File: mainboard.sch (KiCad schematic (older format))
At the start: 42 parts

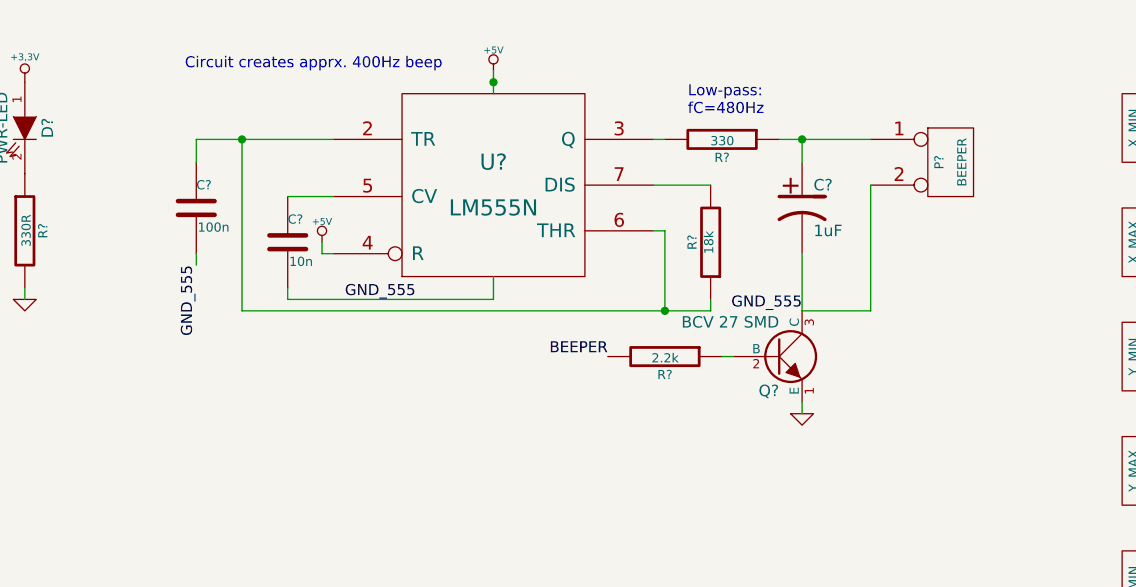
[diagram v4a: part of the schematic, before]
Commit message: Removed 555-Timer-Circuit. Added Opamp to drive beeper.
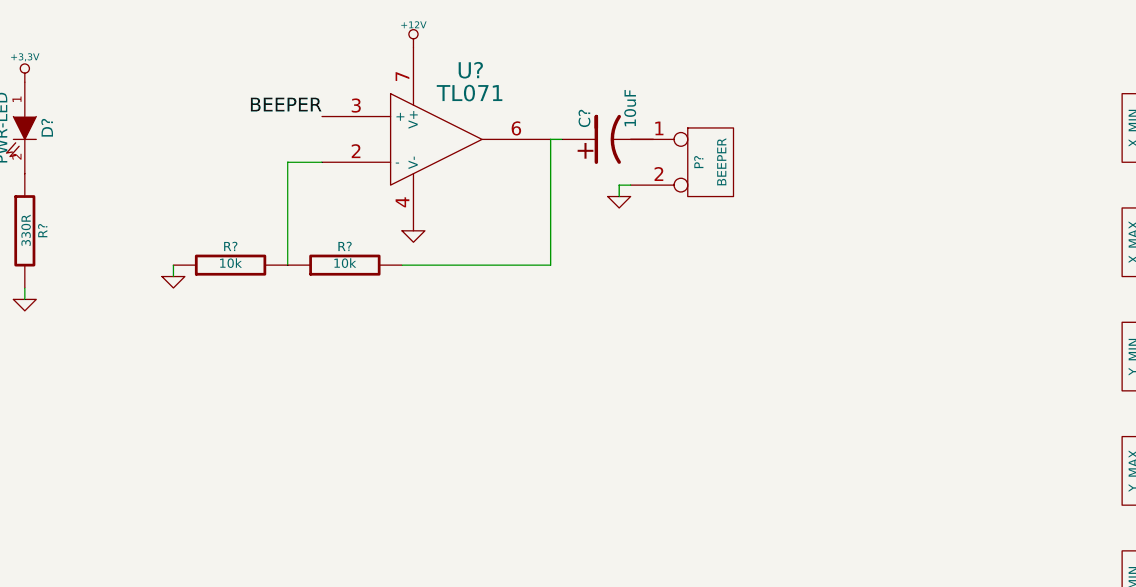
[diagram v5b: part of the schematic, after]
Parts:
- removed C?: 1uF, ~, symbol CP1
- removed C?: 100n, ~, symbol C
- removed C?: 10n, ~, symbol C
- removed P?: BEEPER, symbol CONN_2
- removed Q?: BCV 27 SMD, symbol NPN
- removed R?: 330, symbol R
- removed R?: 18k, symbol R
- removed R?: 2.2k, symbol R
- removed U?: LM555N, symbol LM555N
- added C?: 10uF, ~, symbol CP1
- added P?: BEEPER, symbol CONN_2
- added R? (x2): 10k, symbol R
- added U?: TL071, symbol TL071
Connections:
- net labels removed: GND_555
- wire segments 170 -> 154
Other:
- note removed: "Circuit creates apprx. 400Hz beep"
- note removed: "Low-pass:\nfC=480Hz"
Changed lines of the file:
@@
 Connection ~ 9800 5550
 $Comp
-L LM555N U?
-U 1 1 53348D69
-P 5150 1350
-F 0 "U?" H 5150 1450 70  0000 C CNN
-F 1 "LM555N" H 5150 1250 70  0000 C CNN
-F 2 "" H 5150 1350 60  0000 C CNN
-F 3 "" H 5150 1350 60  0000 C CNN
-	1    5150 1350
+L TL071 U?
+U 1 1 5335F113
+P 4900 1150
+F 0 "U?" H 5050 1450 70  0000 C CNN
+F 1 "TL071" H 5050 1350 70  0000 C CNN
+F 2 "" H 4900 1150 60  0000 C CNN
+F 3 "" H 4900 1150 60  0000 C CNN
+	1    4900 1150
+	1    0    0    -1
+$EndComp
+$Comp
+L R R?
+U 1 1 5335F295
+P 4000 1700
+F 0 "R?" V 4080 1700 40  0000 C CNN
+F 1 "10k" V 4007 1701 40  0000 C CNN
+F 2 "" V 3930 1700 30  0000 C CNN
+F 3 "" H 4000 1700 30  0000 C CNN
+	1    4000 1700
+	0    -1   -1   0
+$EndComp
+Wire Wire Line
+	4250 1250 4400 1250
+$Comp
+L GND #PWR?
+U 1 1 5335F4AF
+P 3750 1750
+F 0 "#PWR?" H 3750 1750 30  0001 C CNN
+F 1 "GND" H 3750 1680 30  0001 C CNN
+F 2 "" H 3750 1750 60  0000 C CNN
+F 3 "" H 3750 1750 60  0000 C CNN
+	1    3750 1750
 	1    0    0    -1
 $EndComp
 Wire Wire Line
-	5150 1850 5150 1750
+	3750 1750 3750 1700
 $Comp
-L +5V #PWR?
-U 1 1 533493FF
-P 5150 850
-F 0 "#PWR?" H 5150 940 20  0001 C CNN
-F 1 "+5V" H 5150 940 30  0000 C CNN
-F 2 "" H 5150 850 60  0000 C CNN
-F 3 "" H 5150 850 60  0000 C CNN
-	1    5150 850
+L R R?
+U 1 1 5335F56E
+P 4500 1700
+F 0 "R?" V 4580 1700 40  0000 C CNN
+F 1 "10k" V 4507 1701 40  0000 C CNN
+F 2 "" V 4430 1700 30  0000 C CNN
+F 3 "" H 4500 1700 30  0000 C CNN
+	1    4500 1700
+	0    -1   -1   0
+$EndComp
+Wire Wire Line
+	4750 1700 5400 1700
+Text Label 4400 1050 2    60   ~ 0
+BEEPER
+$Comp
+L GND #PWR?
+U 1 1 5335F918
+P 4800 1550
+F 0 "#PWR?" H 4800 1550 30  0001 C CNN
+F 1 "GND" H 4800 1480 30  0001 C CNN
+F 2 "" H 4800 1550 60  0000 C CNN
+F 3 "" H 4800 1550 60  0000 C CNN
+	1    4800 1550
+	1    0    0    -1
+$EndComp
+$Comp
+L +12V #PWR?
+U 1 1 5335F923
+P 4800 750
+F 0 "#PWR?" H 4800 700 20  0001 C CNN
+F 1 "+12V" H 4800 850 30  0000 C CNN
+F 2 "" H 4800 750 60  0000 C CNN
+F 3 "" H 4800 750 60  0000 C CNN
+	1    4800 750
+	1    0    0    -1
+$EndComp
+$Comp
+L CONN_2 P?
+U 1 1 5335FA9A
+P 6100 1250
+F 0 "P?" V 6050 1250 40  0000 C CNN
+F 1 "BEEPER" V 6150 1250 40  0000 C CNN
+F 2 "" H 6100 1250 60  0000 C CNN
+F 3 "" H 6100 1250 60  0000 C CNN
+	1    6100 1250
+	1    0    0    -1
+$EndComp
+$Comp
+L CP1 C?
+U 1 1 5335FAAC
+P 5650 1150
+F 0 "C?" H 5700 1250 50  0000 L CNN
+F 1 "10uF" H 5700 1050 50  0000 L CNN
+F 2 "~" H 5650 1150 60  0000 C CNN
+F 3 "~" H 5650 1150 60  0000 C CNN
+	1    5650 1150
+	0    -1   -1   0
+$EndComp
+Wire Wire Line
+	5400 1150 5450 1150
+$Comp
+L GND #PWR?
+U 1 1 5335FB6A
+P 5700 1400
+F 0 "#PWR?" H 5700 1400 30  0001 C CNN
+F 1 "GND" H 5700 1330 30  0001 C CNN
+F 2 "" H 5700 1400 60  0000 C CNN
+F 3 "" H 5700 1400 60  0000 C CNN
+	1    5700 1400
 	1    0    0    -1
 $EndComp
 Wire Wire Line
-	5150 850  5150 950
-Connection ~ 5150 900
-$Comp
-L R R?
-U 1 1 53349632
-P 6150 1150
-F 0 "R?" V 6230 1150 40  0000 C CNN
-F 1 "330" V 6157 1151 40  0000 C CNN
-F 2 "" V 6080 1150 30  0000 C CNN
-F 3 "" H 6150 1150 30  0000 C CNN
-	1    6150 1150
-	0    1    1    0
-$EndComp
+	5700 1400 5700 1350
 Wire Wire Line
-	5900 1150 5850 1150
-$Comp
-L CP1 C?
-U 1 1 533496FD
-P 6500 1450
-F 0 "C?" H 6550 1550 50  0000 L CNN
-F 1 "1uF" H 6550 1350 50  0000 L CNN
-F 2 "~" H 6500 1450 60  0000 C CNN
-F 3 "~" H 6500 1450 60  0000 C CNN
-	1    6500 1450
-	1    0    0    -1
-$EndComp
+	5700 1350 5750 1350
 Wire Wire Line
-	6500 1250 6500 1150
+	5400 1700 5400 1150
 Wire Wire Line
-	6400 1150 6800 1150
-$Comp
-L GND #PWR?
-U 1 1 53349958
-P 6500 2350
-F 0 "#PWR?" H 6500 2350 30  0001 C CNN
-F 1 "GND" H 6500 2280 30  0001 C CNN
-F 2 "" H 6500 2350 60  0000 C CNN
-F 3 "" H 6500 2350 60  0000 C CNN
-	1    6500 2350
-	1    0    0    -1
-$EndComp
-Wire Wire Line
-	6500 1650 6500 1900
-Text Notes 6000 1050 0    48   ~ 0
-Low-pass:\nfC=480Hz
-$Comp
-L CONN_2 P?
-U 1 1 53349A50
-P 7150 1250
-F 0 "P?" V 7100 1250 40  0000 C CNN
-F 1 "BEEPER" V 7200 1250 40  0000 C CNN
-F 2 "" H 7150 1250 60  0000 C CNN
-F 3 "" H 7150 1250 60  0000 C CNN
-	1    7150 1250
-	1    0    0    -1
-$EndComp
-Connection ~ 6500 1150
-Wire Wire Line
-	6800 1350 6800 1900
-$Comp
-L +5V #PWR?
-U 1 1 53349CB7
-P 4400 1600
-F 0 "#PWR?" H 4400 1690 20  0001 C CNN
-F 1 "+5V" H 4400 1690 30  0000 C CNN
-F 2 "" H 4400 1600 60  0000 C CNN
-F 3 "" H 4400 1600 60  0000 C CNN
-	1    4400 1600
-	1    0    0    -1
-$EndComp
-Wire Wire Line
-	4450 1650 4400 1650
-Wire Wire Line
-	4400 1650 4400 1600
-Wire Wire Line
-	5850 1550 5900 1550
-Wire Wire Line
-	5900 1550 5900 1900
-Wire Wire Line
-	4050 1900 6100 1900
-Wire Wire Line
-	4050 1900 4050 1150
-Wire Wire Line
-	3850 1150 4450 1150
-$Comp
-L R R?
-U 1 1 53349E7F
-P 6100 1600
-F 0 "R?" V 6180 1600 40  0000 C CNN
-F 1 "18k" V 6107 1601 40  0000 C CNN
-F 2 "" V 6030 1600 30  0000 C CNN
-F 3 "" H 6100 1600 30  0000 C CNN
-	1    6100 1600
-	-1   0    0    1
-$EndComp
-Wire Wire Line
-	6100 1350 5850 1350
-Wire Wire Line
-	6100 1900 6100 1850
-Connection ~ 5900 1900
-$Comp
-L C C?
-U 1 1 5334A00E
-P 3850 1450
-F 0 "C?" H 3850 1550 40  0000 L CNN
-F 1 "100n" H 3856 1365 40  0000 L CNN
-F 2 "~" H 3888 1300 30  0000 C CNN
-F 3 "~" H 3850 1450 60  0000 C CNN
-	1    3850 1450
-	1    0    0    -1
-$EndComp
-Wire Wire Line
-	3850 1150 3850 1250
-Connection ~ 4050 1150
-$Comp
-L C C?
-U 1 1 5334A561
-P 4250 1600
-F 0 "C?" H 4250 1700 40  0000 L CNN
-F 1 "10n" H 4256 1515 40  0000 L CNN
-F 2 "~" H 4288 1450 30  0000 C CNN
-F 3 "~" H 4250 1600 60  0000 C CNN
-	1    4250 1600
-	1    0    0    -1
-$EndComp
-Wire Wire Line
-	4450 1400 4250 1400
-$Comp
-L NPN Q?
-U 1 1 5334AB92
-P 6400 2100
-F 0 "Q?" H 6400 1950 50  0000 R CNN
-F 1 "BCV 27 SMD" H 6400 2250 50  0000 R CNN
-F 2 "" H 6400 2100 60  0000 C CNN
-F 3 "" H 6400 2100 60  0000 C CNN
-	1    6400 2100
-	1    0    0    -1
-$EndComp
-Wire Wire Line
-	6500 2300 6500 2350
-Wire Wire Line
-	6800 1900 6500 1900
-Text Label 6500 1900 2    48   ~ 0
-GND_555
-Text Label 4500 1850 0    48   ~ 0
-GND_555
-Wire Wire Line
-	4250 1850 4250 1800
-Wire Wire Line
-	4250 1850 5150 1850
-Text Label 3850 1700 3    48   ~ 0
-GND_555
-Wire Wire Line
-	3850 1700 3850 1650
-$Comp
-L R R?
-U 1 1 5334B74A
-P 5900 2100
-F 0 "R?" V 5980 2100 40  0000 C CNN
-F 1 "2.2k" V 5907 2101 40  0000 C CNN
-F 2 "" V 5830 2100 30  0000 C CNN
-F 3 "" H 5900 2100 30  0000 C CNN
-	1    5900 2100
-	0    1    1    0
-$EndComp
-Wire Wire Line
-	6150 2100 6200 2100
-Text Label 5650 2100 2    48   ~ 0
-BEEPER
-Text Notes 3800 850  0    48   ~ 0
-Circuit creates apprx. 400Hz beep
+	4250 1250 4250 1700
 $EndSCHEMATC

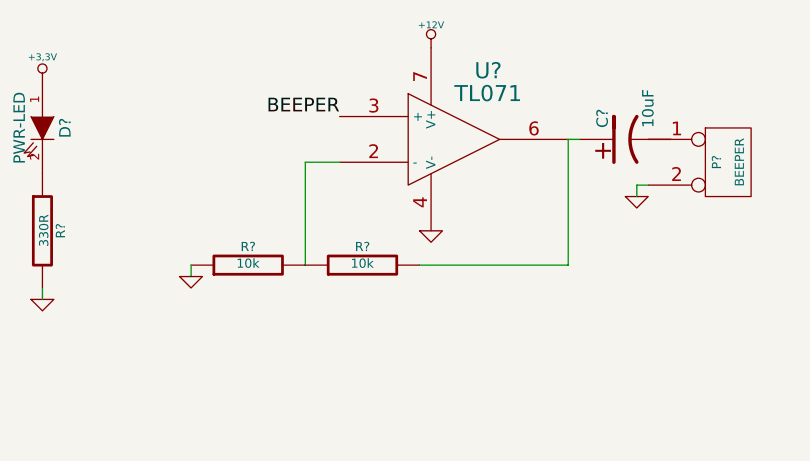
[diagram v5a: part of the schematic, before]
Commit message: Changed OpAmp to NE 4558D SMD
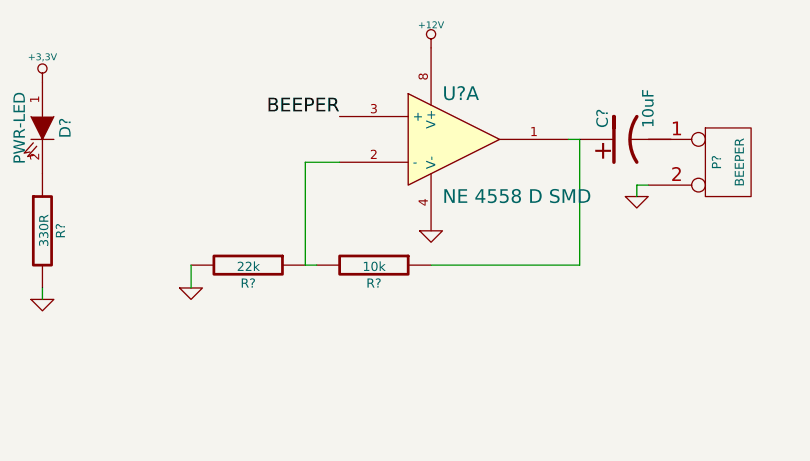
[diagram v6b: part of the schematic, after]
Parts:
- removed R? (x2): 10k, symbol R
- removed U?: TL071, symbol TL071
- added R?: 22k, symbol R
- added R?: 10k, symbol R
- added U?: NE 4558 D SMD, symbol TL082
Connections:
- wire segments 154 -> 155
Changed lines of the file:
@@
 	9800 5350 9800 5550
 Connection ~ 9800 5550
-$Comp
-L TL071 U?
-U 1 1 5335F113
-P 4900 1150
-F 0 "U?" H 5050 1450 70  0000 C CNN
-F 1 "TL071" H 5050 1350 70  0000 C CNN
-F 2 "" H 4900 1150 60  0000 C CNN
-F 3 "" H 4900 1150 60  0000 C CNN
-	1    4900 1150
-	1    0    0    -1
-$EndComp
-$Comp
-L R R?
-U 1 1 5335F295
-P 4000 1700
-F 0 "R?" V 4080 1700 40  0000 C CNN
-F 1 "10k" V 4007 1701 40  0000 C CNN
-F 2 "" V 3930 1700 30  0000 C CNN
-F 3 "" H 4000 1700 30  0000 C CNN
-	1    4000 1700
-	0    -1   -1   0
-$EndComp
 Wire Wire Line
 	4250 1250 4400 1250
-$Comp
-L GND #PWR?
-U 1 1 5335F4AF
-P 3750 1750
-F 0 "#PWR?" H 3750 1750 30  0001 C CNN
-F 1 "GND" H 3750 1680 30  0001 C CNN
-F 2 "" H 3750 1750 60  0000 C CNN
-F 3 "" H 3750 1750 60  0000 C CNN
-	1    3750 1750
-	1    0    0    -1
-$EndComp
-Wire Wire Line
-	3750 1750 3750 1700
-$Comp
-L R R?
-U 1 1 5335F56E
-P 4500 1700
-F 0 "R?" V 4580 1700 40  0000 C CNN
-F 1 "10k" V 4507 1701 40  0000 C CNN
-F 2 "" V 4430 1700 30  0000 C CNN
-F 3 "" H 4500 1700 30  0000 C CNN
-	1    4500 1700
-	0    -1   -1   0
-$EndComp
-Wire Wire Line
-	4750 1700 5400 1700
 Text Label 4400 1050 2    60   ~ 0
 BEEPER
@@
 Wire Wire Line
 	5700 1350 5750 1350
+$Comp
+L R R?
+U 1 1 5336F8FA
+P 4000 1700
+F 0 "R?" V 4080 1700 40  0000 C CNN
+F 1 "22k" V 4007 1701 40  0000 C CNN
+F 2 "" V 3930 1700 30  0000 C CNN
+F 3 "" H 4000 1700 30  0000 C CNN
+	1    4000 1700
+	0    1    1    0
+$EndComp
+$Comp
+L GND #PWR?
+U 1 1 5336F905
+P 3750 1800
+F 0 "#PWR?" H 3750 1800 30  0001 C CNN
+F 1 "GND" H 3750 1730 30  0001 C CNN
+F 2 "" H 3750 1800 60  0000 C CNN
+F 3 "" H 3750 1800 60  0000 C CNN
+	1    3750 1800
+	1    0    0    -1
+$EndComp
 Wire Wire Line
-	5400 1700 5400 1150
+	3750 1800 3750 1700
 Wire Wire Line
 	4250 1250 4250 1700
+Wire Wire Line
+	5450 1150 5450 1700
+$Comp
+L R R?
+U 1 1 5336FBE0
+P 4550 1700
+F 0 "R?" V 4630 1700 40  0000 C CNN
+F 1 "10k" V 4557 1701 40  0000 C CNN
+F 2 "" V 4480 1700 30  0000 C CNN
+F 3 "" H 4550 1700 30  0000 C CNN
+	1    4550 1700
+	0    1    1    0
+$EndComp
+Wire Wire Line
+	4250 1700 4300 1700
+Wire Wire Line
+	5450 1700 4800 1700
+$Comp
+L TL082 U?
+U 1 1 5337003F
+P 4900 1150
+F 0 "U?" H 4850 1350 60  0000 L CNN
+F 1 "NE 4558 D SMD" H 4850 900 60  0000 L CNN
+F 2 "" H 4900 1150 60  0000 C CNN
+F 3 "" H 4900 1150 60  0000 C CNN
+	1    4900 1150
+	1    0    0    -1
+$EndComp
 $EndSCHEMATC

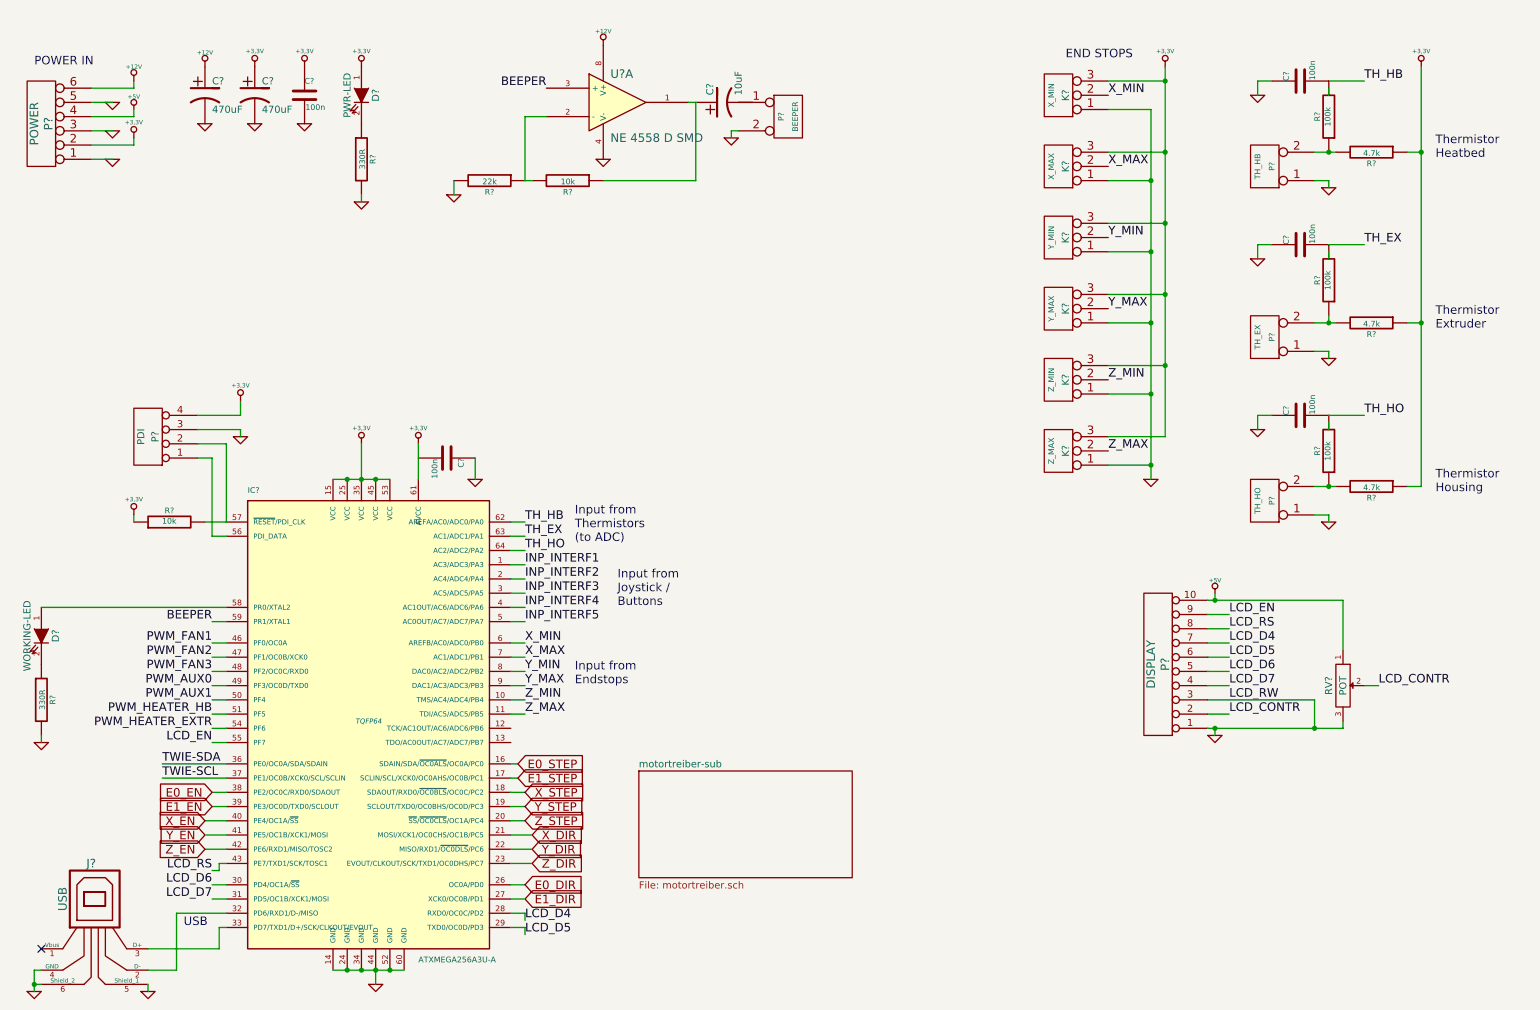
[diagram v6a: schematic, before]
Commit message: Calculated resistor values for thermistor and changed them in the schematic
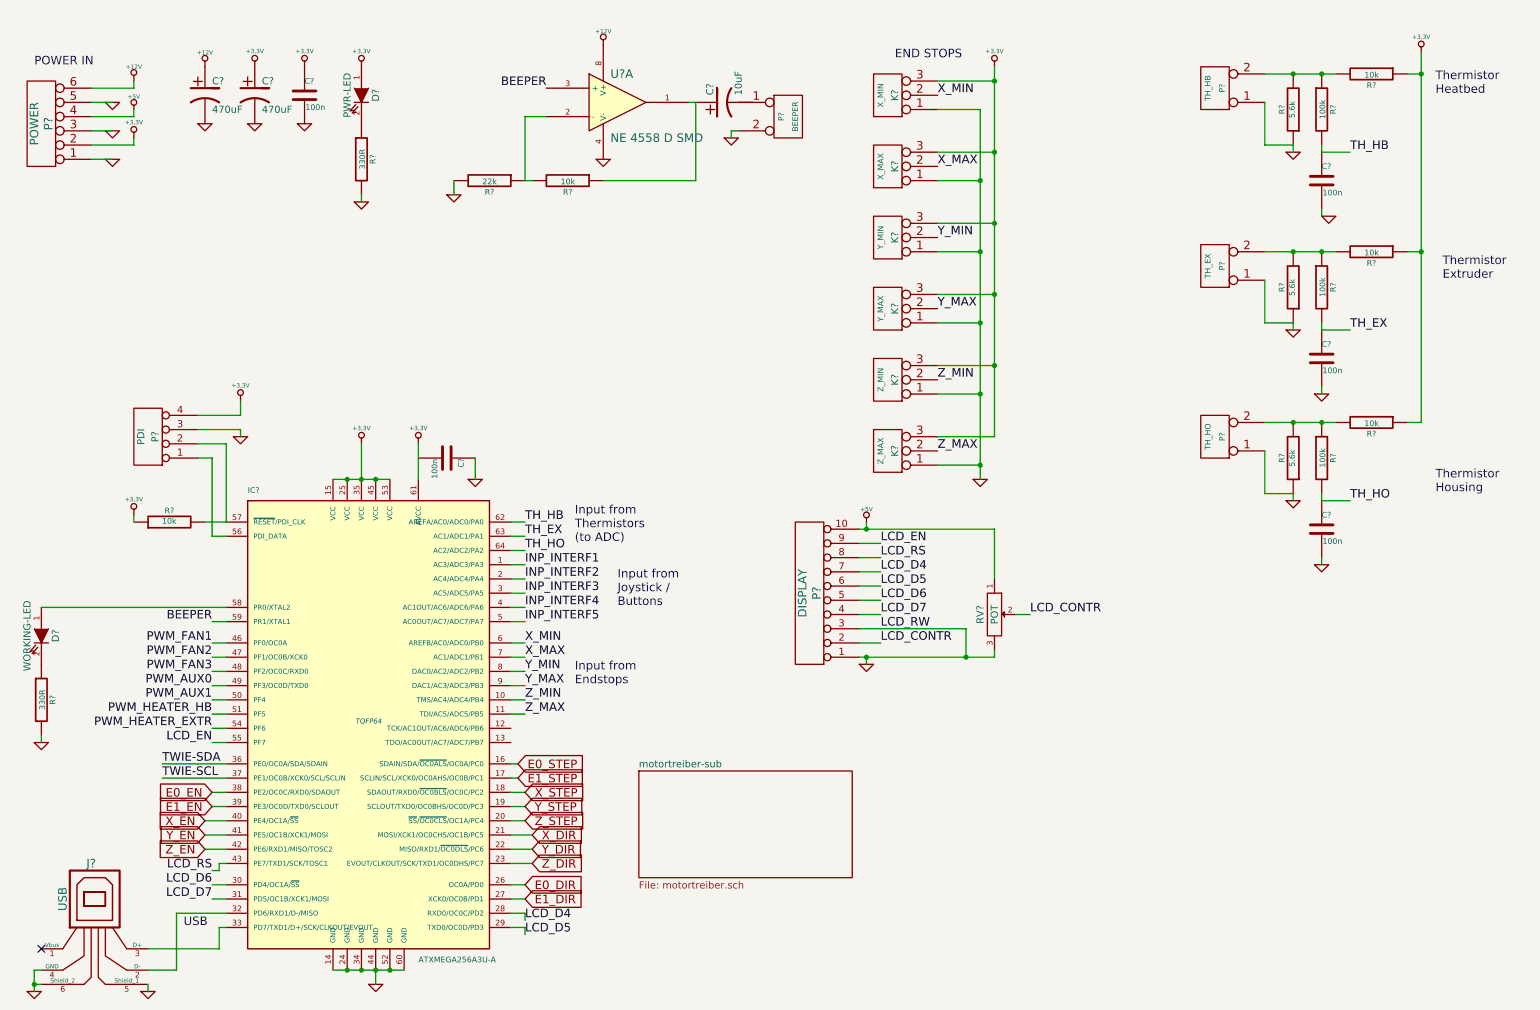
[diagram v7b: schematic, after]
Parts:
- removed C? (x2): 100n, symbol C
- removed P?: TH_EX, symbol CONN_2
- removed P?: TH_HO, symbol CONN_2
- removed R? (x2): 4.7k, symbol R
- removed R? (x2): 100k, symbol R
- added C? (x2): 100n, symbol C
- added P?: TH_EX, symbol CONN_2
- added P?: TH_HO, symbol CONN_2
- added R? (x3): 5.6k, symbol R
- added R? (x2): 10k, symbol R
- added R? (x2): 100k, symbol R
- R?: value 4.7k -> 10k
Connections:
- wire segments 155 -> 154
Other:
- moved on the sheet: C?, K?, P?, R?, RV?
